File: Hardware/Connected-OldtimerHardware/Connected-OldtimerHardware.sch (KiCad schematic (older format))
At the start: 18 parts, among them J1 CAN_Bus_Connector, J2 MainConnector, J3 NextionConnector, Q1 2N3906, U1 ParticleElectron, U2 TSR_2-2450, U3 CANTranceiverModule, U4 AdafruitFRAM, U5 AdafruitUltimateGPS, U6 MotionSensor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

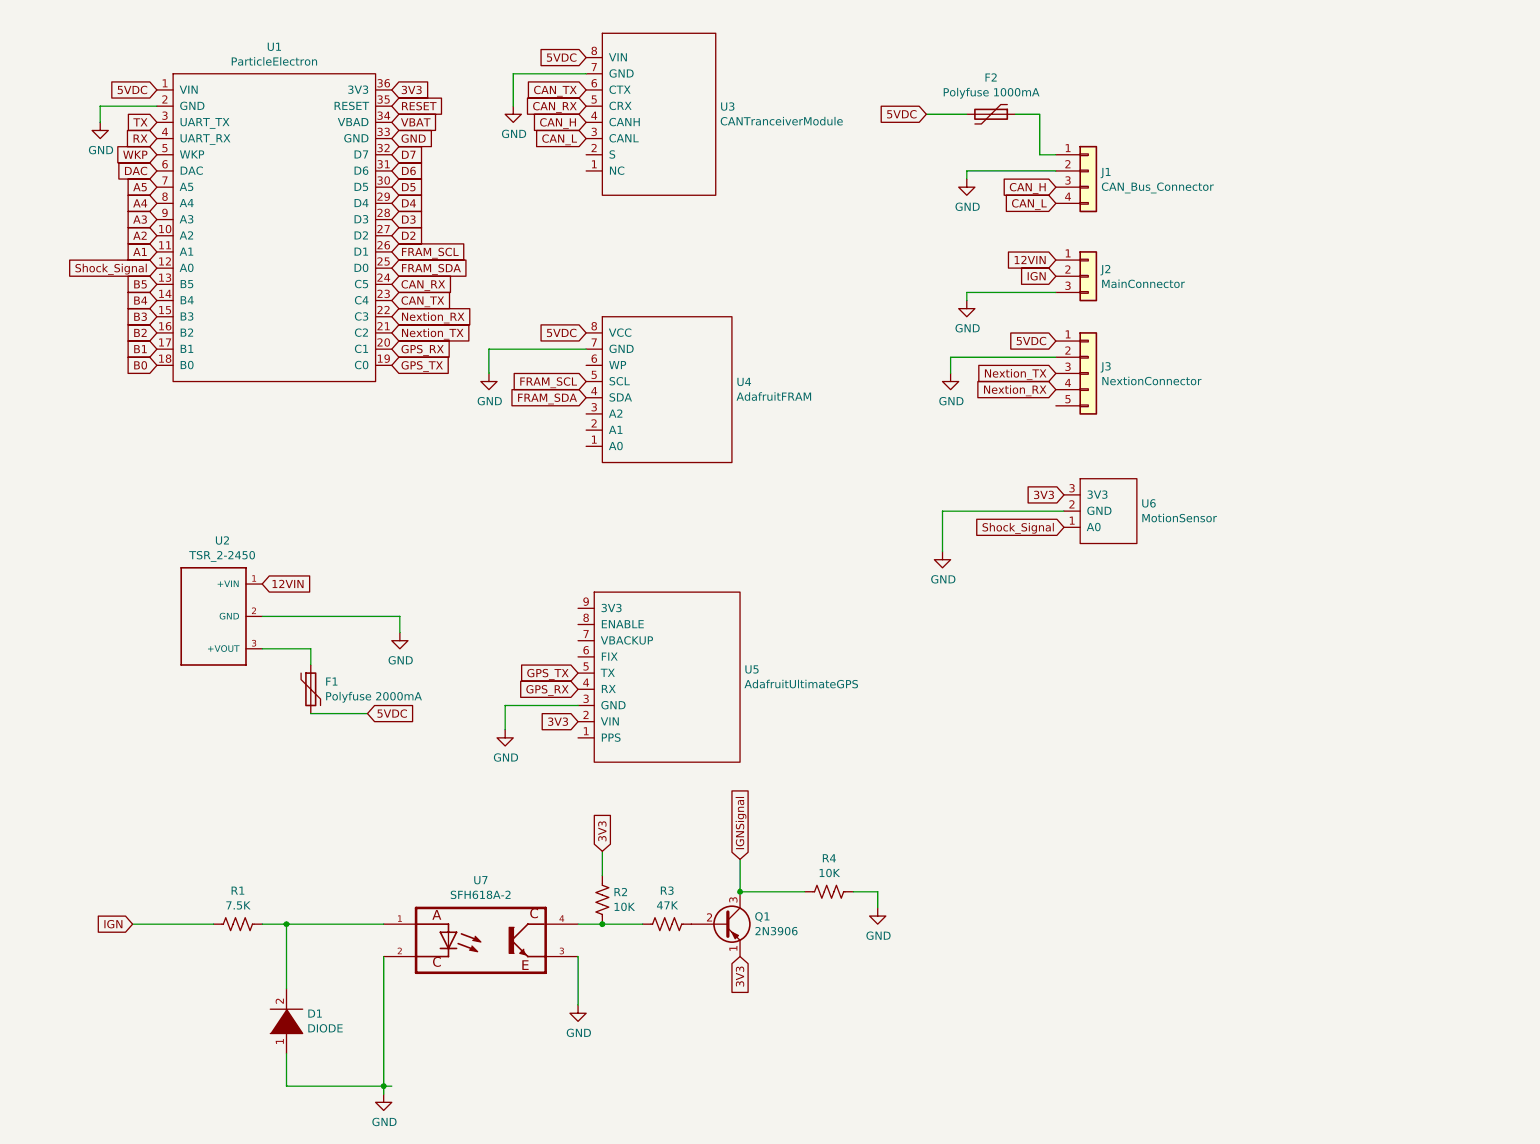
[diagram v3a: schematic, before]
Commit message: redid Regulator Footprint
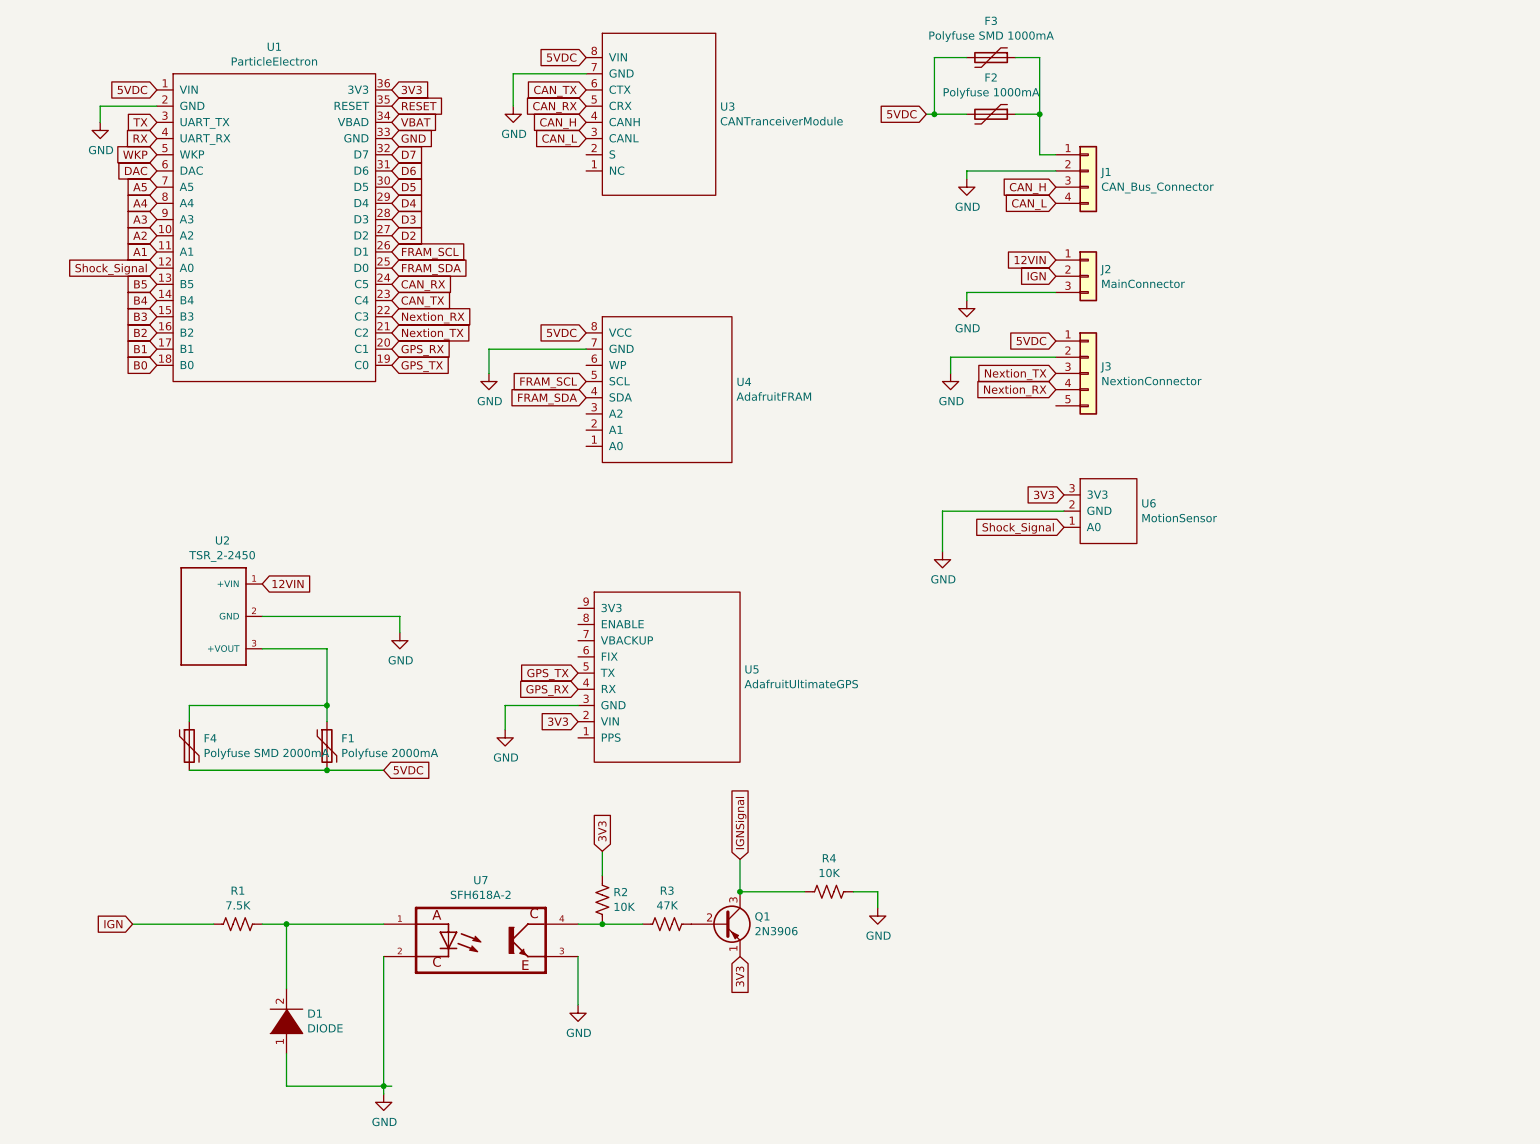
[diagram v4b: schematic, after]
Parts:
- added F3: Polyfuse SMD 1000mA, Capacitor_SMD:C_1210_3225Metric_Pad1.42x2.65mm_HandSolder, symbol Device:Polyfuse
- added F4: Polyfuse SMD 2000mA, Fuse:Fuse_Littelfuse-LVR200, symbol Device:Polyfuse
- U2: footprint SIP750W46P254L1400H1010Q3 -> heathsfootprints:heathsTRS_2_2450
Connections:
- net 5VDC: now also F3.2, F4.2
- net at F2.1, J1.1 (Pin_1): now also F3.1
- net at F1.1, U2.3 (+VOUT): now also F4.1
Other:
- moved on the sheet: F1
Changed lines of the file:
@@
 F 0 "U2" H 1905 4767 50  0000 C CNN
 F 1 "TSR_2-2450" H 1905 4676 50  0000 C CNN
-F 2 "SIP750W46P254L1400H1010Q3" H 1850 4300 50  0001 L BNN
+F 2 "heathsfootprints:heathsTRS_2_2450" H 1850 4300 50  0001 L BNN
 F 3 "SIP-3 Tracopower" H 1850 4300 50  0001 L BNN
 F 4 "TSR 2-2450" H 1850 4300 50  0001 L BNN "Field4"
@@
 Text GLabel 2150 4100 2    50   Input ~ 0
 12VIN
-Text GLabel 2800 4900 2    50   Input ~ 0
+Text GLabel 2900 5250 2    50   Input ~ 0
 5VDC
 $Comp
@@
 $EndComp
 Wire Wire Line
-	6500 1200 6250 1200
+	6500 1200 6300 1200
 Wire Wire Line
 	7050 1450 6950 1450
@@
 L Device:Polyfuse F1
 U 1 1 5D6ED997
-P 2450 4750
-F 0 "F1" H 2538 4796 50  0000 L CNN
-F 1 "Polyfuse 2000mA" H 2538 4705 50  0000 L CNN
-F 2 "Fuse:Fuse_Littelfuse-LVR200" H 2500 4550 50  0001 L CNN
-F 3 "~" H 2450 4750 50  0001 C CNN
-	1    2450 4750
-	1    0    0    -1
-$EndComp
-Wire Wire Line
-	2800 4900 2450 4900
-Wire Wire Line
-	2450 4600 2450 4500
-Wire Wire Line
-	2450 4500 2150 4500
+P 2550 5100
+F 0 "F1" H 2638 5146 50  0000 L CNN
+F 1 "Polyfuse 2000mA" H 2638 5055 50  0000 L CNN
+F 2 "Fuse:Fuse_Littelfuse-LVR200" H 2600 4900 50  0001 L CNN
+F 3 "~" H 2550 5100 50  0001 C CNN
+	1    2550 5100
+	1    0    0    -1
+$EndComp
+Wire Wire Line
+	2900 5250 2550 5250
 Wire Wire Line
 	6350 3650 7100 3650
 Wire Wire Line
 	3550 2650 4150 2650
+$Comp
+L Device:Polyfuse F3
+U 1 1 5D6F203B
+P 6650 850
+F 0 "F3" V 6425 850 50  0000 C CNN
+F 1 "Polyfuse SMD 1000mA" V 6516 850 50  0000 C CNN
+F 2 "Capacitor_SMD:C_1210_3225Metric_Pad1.42x2.65mm_HandSolder" H 6700 650 50  0001 L CNN
+F 3 "~" H 6650 850 50  0001 C CNN
+	1    6650 850
+	0    1    1    0
+$EndComp
+Wire Wire Line
+	6300 850  6300 1200
+Wire Wire Line
+	6300 850  6500 850
+Connection ~ 6300 1200
+Wire Wire Line
+	6300 1200 6250 1200
+Wire Wire Line
+	6800 850  6950 850
+Wire Wire Line
+	6950 850  6950 1200
+Connection ~ 6950 1200
+$Comp
+L Device:Polyfuse F4
+U 1 1 5D6F5FCB
+P 1700 5100
+F 0 "F4" H 1788 5146 50  0000 L CNN
+F 1 "Polyfuse SMD 2000mA" H 1788 5055 50  0000 L CNN
+F 2 "Fuse:Fuse_Littelfuse-LVR200" H 1750 4900 50  0001 L CNN
+F 3 "~" H 1700 5100 50  0001 C CNN
+	1    1700 5100
+	1    0    0    -1
+$EndComp
+Wire Wire Line
+	1700 4950 1700 4850
+Wire Wire Line
+	2150 4500 2550 4500
+Wire Wire Line
+	2550 4500 2550 4850
+Wire Wire Line
+	1700 4850 2550 4850
+Connection ~ 2550 4850
+Wire Wire Line
+	2550 4850 2550 4950
+Wire Wire Line
+	2550 5250 1700 5250
+Connection ~ 2550 5250
 $EndSCHEMATC

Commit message: layout v1
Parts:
- added J?: Conn_01x04, symbol Connector_Generic:Conn_01x04
- F4: footprint Fuse:Fuse_Littelfuse-LVR200 -> Capacitor_SMD:C_1210_3225Metric_Pad1.42x2.65mm_HandSolder
- J1: footprint Connector_JST:JST_EH_B04B-EH-A_1x04_P2.50mm_Vertical -> Connector_JST:JST_XH_B04B-XH-A_1x04_P2.50mm_Vertical
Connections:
- net WKP is gone; now on net Shock_Signal: U1.5 (WKP)
- net GND: now also J?.4 (Pin_4)
- net Shock_Signal: no longer U1.12 (A0)
- net A1: no longer names the net of U1.11 (A1)
- net A2: no longer names the net of U1.10 (A2)
- net A3 renamed AUX_3
- net AUX_3: now also J?.3 (Pin_3)
- net A4: no longer names the net of U1.8 (A4)
- net A5: no longer names the net of U1.7 (A5)
- net B0: no longer names the net of U1.18 (B0)
- net B1: no longer names the net of U1.17 (B1)
- net B2 renamed AUX_2
- net AUX_2: now also J?.2 (Pin_2)
- net B3 renamed AUX_1
- net AUX_1: now also J?.1 (Pin_1)
- net B4: no longer names the net of U1.14 (B4)
- net B5: no longer names the net of U1.13 (B5)
- net D2: no longer names the net of U1.27 (D2)
- net D3: no longer names the net of U1.28 (D3)
- net D4: no longer names the net of U1.29 (D4)
- net D5: no longer names the net of U1.30 (D5)
- net D6: no longer names the net of U1.31 (D6)
- net D7: no longer names the net of U1.32 (D7)
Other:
- moved on the sheet: U6
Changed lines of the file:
@@
 Text GLabel 1500 1350 0    50   Input ~ 0
 RX
-Text GLabel 1500 1450 0    50   Input ~ 0
-WKP
 Text GLabel 1500 1550 0    50   Input ~ 0
 DAC
-Text GLabel 1500 1650 0    50   Input ~ 0
-A5
-Text GLabel 1500 1750 0    50   Input ~ 0
-A4
-Text GLabel 1500 1850 0    50   Input ~ 0
-A3
-Text GLabel 1500 1950 0    50   Input ~ 0
-A2
-Text GLabel 1500 2050 0    50   Input ~ 0
-A1
-Text GLabel 1500 2150 0    50   Input ~ 0
+Text GLabel 1500 1450 0    50   Input ~ 0
 Shock_Signal
-Text GLabel 1500 2250 0    50   Input ~ 0
-B5
-Text GLabel 1500 2350 0    50   Input ~ 0
-B4
-Text GLabel 1500 2450 0    50   Input ~ 0
-B3
-Text GLabel 1500 2550 0    50   Input ~ 0
-B2
-Text GLabel 1500 2650 0    50   Input ~ 0
-B1
-Text GLabel 1500 2750 0    50   Input ~ 0
-B0
 Text GLabel 4150 2550 0    50   Input ~ 0
 5VDC
@@
 F 0 "J1" H 7330 1542 50  0000 L CNN
 F 1 "CAN_Bus_Connector" H 7330 1451 50  0000 L CNN
-F 2 "Connector_JST:JST_EH_B04B-EH-A_1x04_P2.50mm_Vertical" H 7250 1550 50  0001 C CNN
+F 2 "Connector_JST:JST_XH_B04B-XH-A_1x04_P2.50mm_Vertical" H 7250 1550 50  0001 C CNN
 F 3 "~" H 7250 1550 50  0001 C CNN
 	1    7250 1550
@@
 Text GLabel 7050 1750 0    50   Input ~ 0
 CAN_L
-Text GLabel 7100 3550 0    50   Input ~ 0
+Text GLabel 7100 5200 0    50   Input ~ 0
 3V3
-Text GLabel 7100 3750 0    50   Input ~ 0
+Text GLabel 7100 5400 0    50   Input ~ 0
 Shock_Signal
 $Comp
@@
 Text GLabel 2950 1350 2    50   Input ~ 0
 GND
-Text GLabel 2950 1450 2    50   Input ~ 0
-D7
-Text GLabel 2950 1550 2    50   Input ~ 0
-D6
-Text GLabel 2950 1650 2    50   Input ~ 0
-D5
-Text GLabel 2950 1750 2    50   Input ~ 0
-D4
-Text GLabel 2950 1850 2    50   Input ~ 0
-D3
-Text GLabel 2950 1950 2    50   Input ~ 0
-D2
 Text GLabel 2950 2050 2    50   Input ~ 0
 FRAM_SCL
@@
 L Connected-OldtimerHardware-rescue:MotionSensor-HeathsComponents U6
 U 1 1 5D6D1163
-P 7500 3650
-F 0 "U6" H 7577 3696 50  0000 L CNN
-F 1 "MotionSensor" H 7577 3605 50  0000 L CNN
-F 2 "heathsfootprints:ShockSensor" H 7500 3650 50  0001 C CNN
-F 3 "" H 7500 3650 50  0001 C CNN
-	1    7500 3650
+P 7500 5300
+F 0 "U6" H 7577 5346 50  0000 L CNN
+F 1 "MotionSensor" H 7577 5255 50  0000 L CNN
+F 2 "heathsfootprints:ShockSensor" H 7500 5300 50  0001 C CNN
+F 3 "" H 7500 5300 50  0001 C CNN
+	1    7500 5300
 	1    0    0    -1
 $EndComp
@@
 L power:GND #PWR0109
 U 1 1 5D6E51A5
-P 6350 3900
-F 0 "#PWR0109" H 6350 3650 50  0001 C CNN
-F 1 "GND" H 6355 3727 50  0000 C CNN
-F 2 "" H 6350 3900 50  0001 C CNN
-F 3 "" H 6350 3900 50  0001 C CNN
-	1    6350 3900
-	1    0    0    -1
-$EndComp
-Wire Wire Line
-	6350 3650 6350 3900
+P 6350 5550
+F 0 "#PWR0109" H 6350 5300 50  0001 C CNN
+F 1 "GND" H 6355 5377 50  0000 C CNN
+F 2 "" H 6350 5550 50  0001 C CNN
+F 3 "" H 6350 5550 50  0001 C CNN
+	1    6350 5550
+	1    0    0    -1
+$EndComp
+Wire Wire Line
+	6350 5300 6350 5550
 Wire Wire Line
 	7050 2700 6400 2700
@@
 L power:GND #PWR0112
 U 1 1 5D6E6E4F
-P 1150 1250
-F 0 "#PWR0112" H 1150 1000 50  0001 C CNN
-F 1 "GND" H 1155 1077 50  0000 C CNN
-F 2 "" H 1150 1250 50  0001 C CNN
-F 3 "" H 1150 1250 50  0001 C CNN
-	1    1150 1250
-	1    0    0    -1
-$EndComp
-Wire Wire Line
-	1500 1150 1150 1150
-Wire Wire Line
-	1150 1150 1150 1250
+P 700 1250
+F 0 "#PWR0112" H 700 1000 50  0001 C CNN
+F 1 "GND" H 705 1077 50  0000 C CNN
+F 2 "" H 700 1250 50  0001 C CNN
+F 3 "" H 700 1250 50  0001 C CNN
+	1    700  1250
+	1    0    0    -1
+$EndComp
+Wire Wire Line
+	700  1150 700  1250
 $Comp
 L Device:Polyfuse F2
@@
 	2900 5250 2550 5250
 Wire Wire Line
-	6350 3650 7100 3650
+	6350 5300 7100 5300
 Wire Wire Line
 	3550 2650 4150 2650
@@
 F 0 "F4" H 1788 5146 50  0000 L CNN
 F 1 "Polyfuse SMD 2000mA" H 1788 5055 50  0000 L CNN
-F 2 "Fuse:Fuse_Littelfuse-LVR200" H 1750 4900 50  0001 L CNN
+F 2 "Capacitor_SMD:C_1210_3225Metric_Pad1.42x2.65mm_HandSolder" H 1750 4900 50  0001 L CNN
 F 3 "~" H 1700 5100 50  0001 C CNN
 	1    1700 5100
@@
 	2550 5250 1700 5250
 Connection ~ 2550 5250
+$Comp
+L power:GND #PWR?
+U 1 1 5D70C303
+P 6900 3750
+F 0 "#PWR?" H 6900 3500 50  0001 C CNN
+F 1 "GND" H 6905 3577 50  0000 C CNN
+F 2 "" H 6900 3750 50  0001 C CNN
+F 3 "" H 6900 3750 50  0001 C CNN
+	1    6900 3750
+	1    0    0    -1
+$EndComp
+Wire Wire Line
+	6900 3750 6900 3600
+Wire Wire Line
+	6900 3600 7050 3600
+Text GLabel 7050 3300 0    50   Input ~ 0
+AUX_1
+Text GLabel 7050 3400 0    50   Input ~ 0
+AUX_2
+Text GLabel 7050 3500 0    50   Input ~ 0
+AUX_3
+Text GLabel 1500 2450 0    50   Input ~ 0
+AUX_1
+Text GLabel 1500 2550 0    50   Input ~ 0
+AUX_2
+Wire Wire Line
+	700  1150 1500 1150
+Text GLabel 1500 1850 0    50   Input ~ 0
+AUX_3
+$Comp
+L Connector_Generic:Conn_01x04 J?
+U 1 1 5D717741
+P 7250 3400
+F 0 "J?" H 7330 3392 50  0000 L CNN
+F 1 "Conn_01x04" H 7330 3301 50  0000 L CNN
+F 2 "" H 7250 3400 50  0001 C CNN
+F 3 "~" H 7250 3400 50  0001 C CNN
+	1    7250 3400
+	1    0    0    -1
+$EndComp
 $EndSCHEMATC

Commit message: all connections except ground and 5v
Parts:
- added 1uF1: C, Capacitor_THT:C_Disc_D8.0mm_W2.5mm_P5.00mm, symbol Device:C
- added 31K1, 4.7k1: R_US, Resistor_THT:R_Axial_DIN0207_L6.3mm_D2.5mm_P10.16mm_Horizontal, symbol Device:R_US
- added D2: D_Zener, Diode_THT:D_DO-41_SOD81_P7.62mm_Horizontal, symbol Device:D_Zener
- J3: footprint Connector_JST:JST_XH_B05B-XH-A_1x05_P2.50mm_Vertical -> Connector_JST:JST_XH_S05B-XH-A-1_1x05_P2.50mm_Horizontal
- J4: renamed from J?; value Conn_01x04 -> AUXConnector; footprint (none) -> Connector_JST:JST_XH_B04B-XH-A_1x04_P2.50mm_Vertical
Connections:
- net 12VIN: now also 31K1.1
- net 3V3: now also U4.8 (VCC)
- net 5VDC: no longer U4.8 (VCC)
- net GND: now also 1uF1.2, 4.7k1.2, D2.2 (A)
- net VMON: now reaches U1.12 (A0)
- net VMON: now also 1uF1.1, 31K1.2, 4.7k1.1, D2.1 (K)
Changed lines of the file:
@@
 Shock_Signal
 Text GLabel 4150 2550 0    50   Input ~ 0
-5VDC
+3V3
 Text GLabel 4150 2850 0    50   Input ~ 0
 FRAM_SCL
@@
 F 0 "J3" H 7330 2842 50  0000 L CNN
 F 1 "NextionConnector" H 7330 2751 50  0000 L CNN
-F 2 "Connector_JST:JST_XH_B05B-XH-A_1x05_P2.50mm_Vertical" H 7250 2800 50  0001 C CNN
+F 2 "Connector_JST:JST_XH_S05B-XH-A-1_1x05_P2.50mm_Horizontal" H 7250 2800 50  0001 C CNN
 F 3 "~" H 7250 2800 50  0001 C CNN
 	1    7250 2800
@@
 Connection ~ 2550 5250
 $Comp
-L power:GND #PWR?
+L power:GND #PWR0113
 U 1 1 5D70C303
 P 6900 3750
-F 0 "#PWR?" H 6900 3500 50  0001 C CNN
+F 0 "#PWR0113" H 6900 3500 50  0001 C CNN
 F 1 "GND" H 6905 3577 50  0000 C CNN
 F 2 "" H 6900 3750 50  0001 C CNN
@@
 AUX_3
 $Comp
-L Connector_Generic:Conn_01x04 J?
+L Connector_Generic:Conn_01x04 J4
 U 1 1 5D717741
 P 7250 3400
-F 0 "J?" H 7330 3392 50  0000 L CNN
-F 1 "Conn_01x04" H 7330 3301 50  0000 L CNN
-F 2 "" H 7250 3400 50  0001 C CNN
+F 0 "J4" H 7330 3392 50  0000 L CNN
+F 1 "AUXConnector" H 7330 3301 50  0000 L CNN
+F 2 "Connector_JST:JST_XH_B04B-XH-A_1x04_P2.50mm_Vertical" H 7250 3400 50  0001 C CNN
 F 3 "~" H 7250 3400 50  0001 C CNN
 	1    7250 3400
 	1    0    0    -1
 $EndComp
+$Comp
+L Device:R_US 31K1
+U 1 1 5D6FDF91
+P 8450 3900
+F 0 "31K1" H 8518 3946 50  0000 L CNN
+F 1 "R_US" H 8518 3855 50  0000 L CNN
+F 2 "Resistor_THT:R_Axial_DIN0207_L6.3mm_D2.5mm_P10.16mm_Horizontal" V 8490 3890 50  0001 C CNN
+F 3 "~" H 8450 3900 50  0001 C CNN
+	1    8450 3900
+	1    0    0    -1
+$EndComp
+$Comp
+L Device:R_US 4.7k1
+U 1 1 5D6FE056
+P 8450 4350
+F 0 "4.7k1" H 8518 4396 50  0000 L CNN
+F 1 "R_US" H 8518 4305 50  0000 L CNN
+F 2 "Resistor_THT:R_Axial_DIN0207_L6.3mm_D2.5mm_P10.16mm_Horizontal" V 8490 4340 50  0001 C CNN
+F 3 "~" H 8450 4350 50  0001 C CNN
+	1    8450 4350
+	1    0    0    -1
+$EndComp
+$Comp
+L Device:D_Zener D2
+U 1 1 5D6FEC30
+P 9150 4350
+F 0 "D2" V 9104 4429 50  0000 L CNN
+F 1 "D_Zener" V 9195 4429 50  0000 L CNN
+F 2 "Diode_THT:D_DO-41_SOD81_P7.62mm_Horizontal" H 9150 4350 50  0001 C CNN
+F 3 "~" H 9150 4350 50  0001 C CNN
+	1    9150 4350
+	0    1    1    0
+$EndComp
+$Comp
+L Device:C 1uF1
+U 1 1 5D6FED32
+P 8850 4350
+F 0 "1uF1" H 8965 4396 50  0000 L CNN
+F 1 "C" H 8965 4305 50  0000 L CNN
+F 2 "Capacitor_THT:C_Disc_D8.0mm_W2.5mm_P5.00mm" H 8888 4200 50  0001 C CNN
+F 3 "~" H 8850 4350 50  0001 C CNN
+	1    8850 4350
+	1    0    0    -1
+$EndComp
+Text GLabel 8250 3750 0    50   Input ~ 0
+12VIN
+Text GLabel 9600 4200 2    50   Input ~ 0
+VMON
+Wire Wire Line
+	8450 4200 8850 4200
+Connection ~ 8850 4200
+Wire Wire Line
+	8850 4200 9150 4200
+Wire Wire Line
+	8450 4200 8450 4050
+Connection ~ 8450 4200
+Wire Wire Line
+	8450 3750 8250 3750
+Wire Wire Line
+	8450 4500 8850 4500
+Wire Wire Line
+	9150 4500 8850 4500
+Connection ~ 8850 4500
+$Comp
+L power:GND #PWR0114
+U 1 1 5D7056BE
+P 8850 4500
+F 0 "#PWR0114" H 8850 4250 50  0001 C CNN
+F 1 "GND" H 8855 4327 50  0000 C CNN
+F 2 "" H 8850 4500 50  0001 C CNN
+F 3 "" H 8850 4500 50  0001 C CNN
+	1    8850 4500
+	1    0    0    -1
+$EndComp
+Wire Wire Line
+	9600 4200 9150 4200
+Connection ~ 9150 4200
+Text GLabel 1500 2150 0    50   Input ~ 0
+VMON
 $EndSCHEMATC
